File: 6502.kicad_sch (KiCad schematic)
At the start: 34 parts, among them J3 Conn_01x40, J4 CPU Control, SW1 Reset, U1 W65C02SxP, U2 AT28C256, U3 HM62256BLP, Y1 1MHz

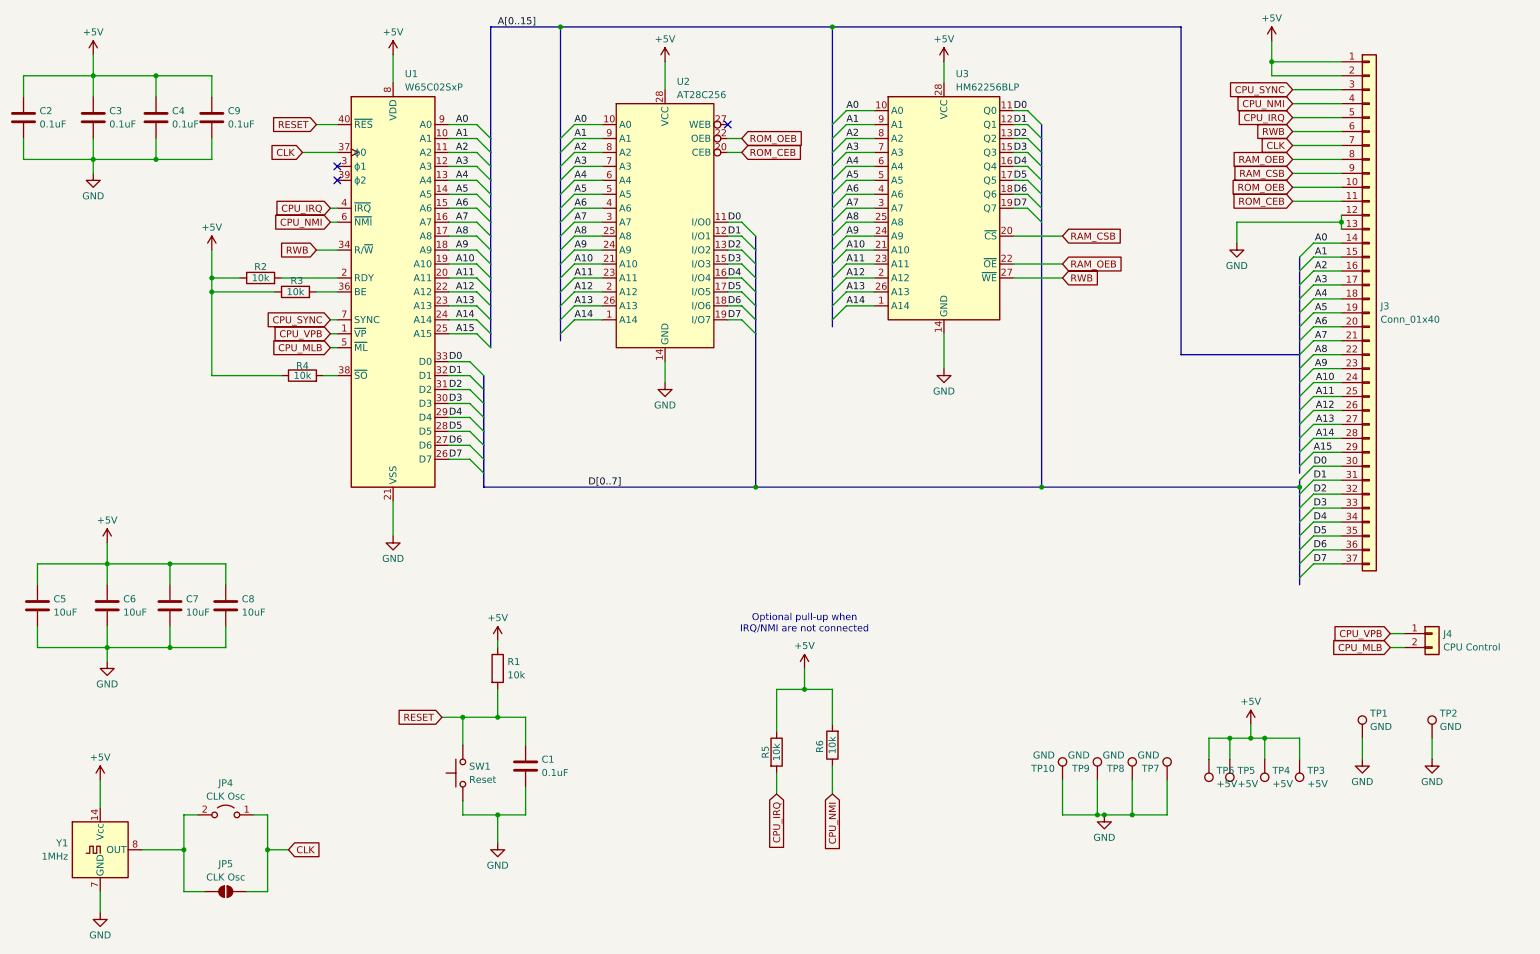
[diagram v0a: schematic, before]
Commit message: Update schematics
Schematics:

- J3: Replace SYNC with RST
- J4: Add SYNC
- Rename CEB do CSB (Chip Enabled -> Chip Select)

PCB:
- Increase GND Polygon min clearance
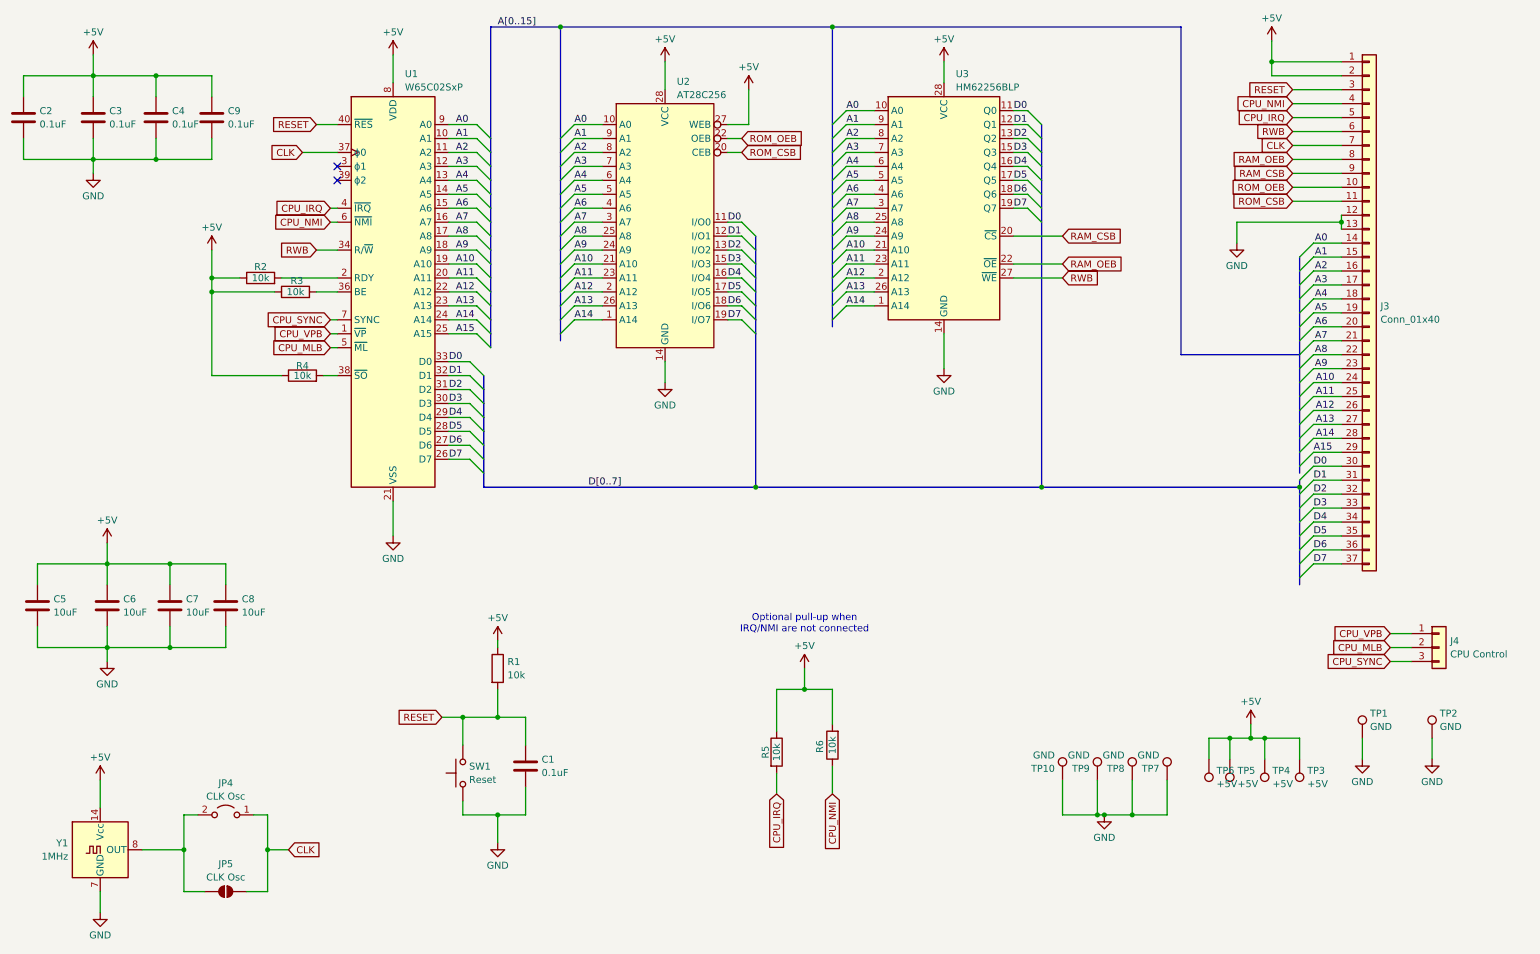
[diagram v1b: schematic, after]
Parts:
- J4: footprint Connector_PinHeader_2.54mm:PinHeader_1x02_P2.54mm_Vertical -> Connector_PinHeader_2.54mm:PinHeader_1x03_P2.54mm_Vertical; symbol Connector_Generic:Conn_01x02 -> Connector_Generic:Conn_01x03
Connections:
- net +5V: now also U2.27 (WEB)
- net CPU_SYNC: now also J4.3 (Pin_3); no longer J3.3 (Pin_3)
- net RESET: now also J3.3 (Pin_3)
- net ROM_CEB renamed ROM_CSB
- no-connect marks 3 -> 2
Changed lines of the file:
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@@
 		(at 73.66 45.72)
 	)
-	(no_connect
-		(at 144.78 35.56)
-	)
 	(bus_entry
 		(at 201.93 50.8)
@@
 		)
 	)
+	(wire
+		(pts
+			(xy 247.65 29.21) (xy 256.54 29.21)
+		)
+		(stroke
+			(width 0)
+			(type default)
+		)
+	)
 	(bus
 		(pts
@@
 	(wire
 		(pts
-			(xy 265.43 128.27) (xy 267.97 128.27)
-		)
-		(stroke
-			(width 0)
-			(type default)
-		)
-	)
-	(wire
-		(pts
 			(xy 251.46 80.01) (xy 256.54 80.01)
 		)
@@
 	(wire
 		(pts
-			(xy 133.35 24.13) (xy 133.35 29.21)
+			(xy 148.59 35.56) (xy 148.59 29.21)
 		)
 		(stroke
@@
 	(wire
 		(pts
-			(xy 247.65 29.21) (xy 256.54 29.21)
+			(xy 133.35 24.13) (xy 133.35 29.21)
 		)
 		(stroke
@@
 	(wire
 		(pts
+			(xy 265.43 130.81) (xy 269.24 130.81)
+		)
+		(stroke
+			(width 0)
+			(type default)
+		)
+	)
+	(wire
+		(pts
 			(xy 116.84 53.34) (xy 121.92 53.34)
 		)
@@
 	(wire
 		(pts
+			(xy 265.43 128.27) (xy 269.24 128.27)
+		)
+		(stroke
+			(width 0)
+			(type default)
+		)
+	)
+	(wire
+		(pts
 			(xy 93.98 50.8) (xy 99.06 50.8)
 		)
@@
 		)
 	)
+	(wire
+		(pts
+			(xy 144.78 35.56) (xy 148.59 35.56)
+		)
+		(stroke
+			(width 0)
+			(type default)
+		)
+	)
 	(bus
 		(pts
@@
 		)
 	)
+	(wire
+		(pts
+			(xy 265.43 133.35) (xy 269.24 133.35)
+		)
+		(stroke
+			(width 0)
+			(type default)
+		)
+	)
 	(bus
 		(pts
@@
 	(wire
 		(pts
-			(xy 265.43 130.81) (xy 267.97 130.81)
-		)
-		(stroke
-			(width 0)
-			(type default)
-		)
-	)
-	(wire
-		(pts
 			(xy 144.78 58.42) (xy 147.32 58.42)
 		)
@@
 		)
 	)
+	(global_label "RESET"
+		(shape input)
+		(at 247.65 29.21 180)
+		(fields_autoplaced yes)
+		(effects
+			(font
+				(size 1.27 1.27)
+			)
+			(justify right)
+		)
+		(property "Intersheetrefs" "${INTERSHEET_REFS}"
+			(at 238.9197 29.21 0)
+			(effects
+				(font
+					(size 1.27 1.27)
+				)
+				(justify right)
+				(hide yes)
+			)
+		)
+	)
 	(global_label "RWB"
 		(shape input)
@@
 	(global_label "CPU_SYNC"
 		(shape input)
-		(at 247.65 29.21 180)
+		(at 265.43 133.35 180)
 		(fields_autoplaced yes)
 		(effects
@@
 		)
 		(property "Intersheetrefs" "${INTERSHEET_REFS}"
-			(at 234.9281 29.21 0)
+			(at 252.7081 133.35 0)
 			(effects
 				(font
@@
 		)
 	)
-	(global_label "ROM_CEB"
+	(global_label "ROM_CSB"
 		(shape input)
 		(at 247.65 49.53 180)
@@
 		)
 		(property "Intersheetrefs" "${INTERSHEET_REFS}"
-			(at 235.9563 49.53 0)
+			(at 235.8958 49.53 0)
 			(effects
 				(font
@@
 		)
 	)
-	(global_label "ROM_CEB"
+	(global_label "ROM_CSB"
 		(shape input)
 		(at 147.32 40.64 0)
@@
 		)
 		(property "Intersheetrefs" "${INTERSHEET_REFS}"
-			(at 159.0137 40.64 0)
+			(at 159.0742 40.64 0)
 			(effects
 				(font
@@
 	)
 	(symbol
-		(lib_id "Connector_Generic:Conn_01x02")
-		(at 273.05 128.27 0)
+		(lib_id "Connector_Generic:Conn_01x03")
+		(at 274.32 130.81 0)
 		(unit 1)
 		(exclude_from_sim no)
@@
 		(fields_autoplaced yes)
 		(property "Reference" "J4"
-			(at 275.082 128.3278 0)
+			(at 276.352 129.5978 0)
 			(effects
 				(font
@@
 		)
 		(property "Value" "CPU Control"
-			(at 275.082 130.7521 0)
+			(at 276.352 132.0221 0)
 			(effects
 				(font
@@
 			)
 		)
-		(property "Footprint" "Connector_PinHeader_2.54mm:PinHeader_1x02_P2.54mm_Vertical"
-			(at 273.05 128.27 0)
+		(property "Footprint" "Connector_PinHeader_2.54mm:PinHeader_1x03_P2.54mm_Vertical"
+			(at 274.32 130.81 0)
 			(effects
 				(font
@@
 		)
 		(property "Datasheet" "~"
-			(at 273.05 128.27 0)
+			(at 274.32 130.81 0)
 			(effects
 				(font
@@
 			)
 		)
-		(property "Description" "Generic connector, single row, 01x02, script generated (kicad-library-utils/schlib/autogen/connector/)"
-			(at 273.05 128.27 0)
+		(property "Description" "Generic connector, single row, 01x03, script generated (kicad-library-utils/schlib/autogen/connector/)"
+			(at 274.32 130.81 0)
 			(effects
 				(font
@@
 		(pin "2"
 		)
+		(pin "3"
+		)
 		(instances
 			(project "6502"
@@
 					(unit 1)
 				)
+			)
+		)
+	)
+	(symbol
+		(lib_id "power:+5V")
+		(at 148.59 29.21 0)
+		(unit 1)
+		(exclude_from_sim no)
+		(in_bom yes)
+		(on_board yes)
+		(dnp no)
+		(fields_autoplaced yes)
+		(property "Reference" "#PWR014"
+			(at 148.59 33.02 0)
+			(effects
+				(font
+					(size 1.27 1.27)
+				)
+				(hide yes)
+			)
+		)
+		(property "Value" "+5V"
+			(at 148.59 25.0769 0)
+			(effects
+				(font
+					(size 1.27 1.27)
+				)
+			)
+		)
+		(property "Footprint" ""
+			(at 148.59 29.21 0)
+			(effects
+				(font
+					(size 1.27 1.27)
+				)
+				(hide yes)
+			)
+		)
+		(property "Datasheet" ""
+			(at 148.59 29.21 0)
+			(effects
+				(font
+					(size 1.27 1.27)
+				)
+				(hide yes)
+			)
+		)
+		(property "Description" "Power symbol creates a global label with name \"+5V\""
+			(at 148.59 29.21 0)
+			(effects
+				(font
+					(size 1.27 1.27)
+				)
+				(hide yes)
+			)
+		)
+		(pin "1"
+		)
+		(instances
+			(project "6502"
+				(path "/b27827ff-d5fb-42df-9ec7-758c6c864402"
+					(reference "#PWR014")
+					(unit 1)
+				)
